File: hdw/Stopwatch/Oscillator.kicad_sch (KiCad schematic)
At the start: 12 parts, among them U401 CD4024, U402 CD4040, X401 ECS-327KE

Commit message: started sch work
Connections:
- net 16Hz_Clock: no longer names the net of U402.5 (Q3)
- net 4Hz_Clock: no longer names the net of U402.2 (Q5)
- net Count_Reset renamed Master_Reset
- no-connect marks 15 -> 17
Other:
- moved on the sheet: C401, C402, C403, C404, R401, R402, R403, R404, X401

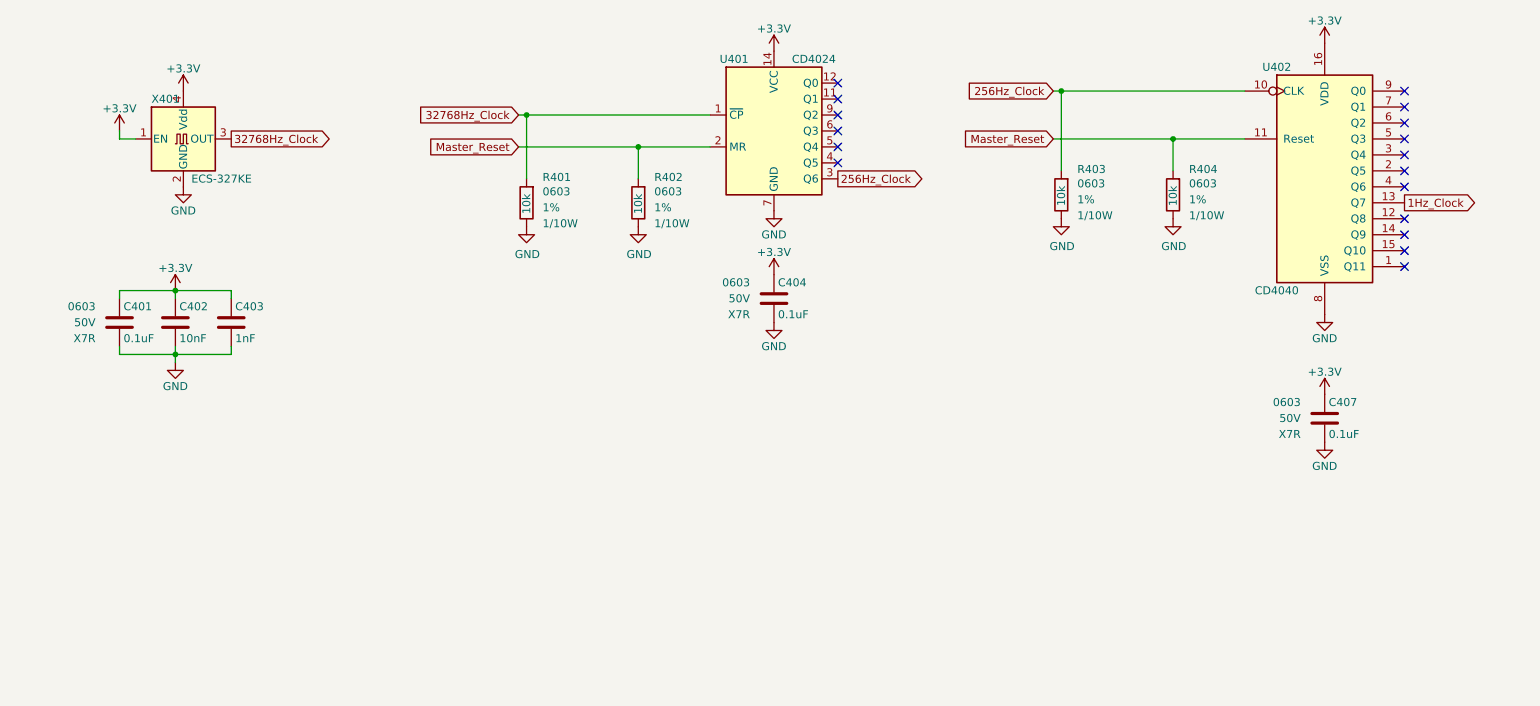
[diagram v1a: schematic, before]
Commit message: adjusted stage sheet
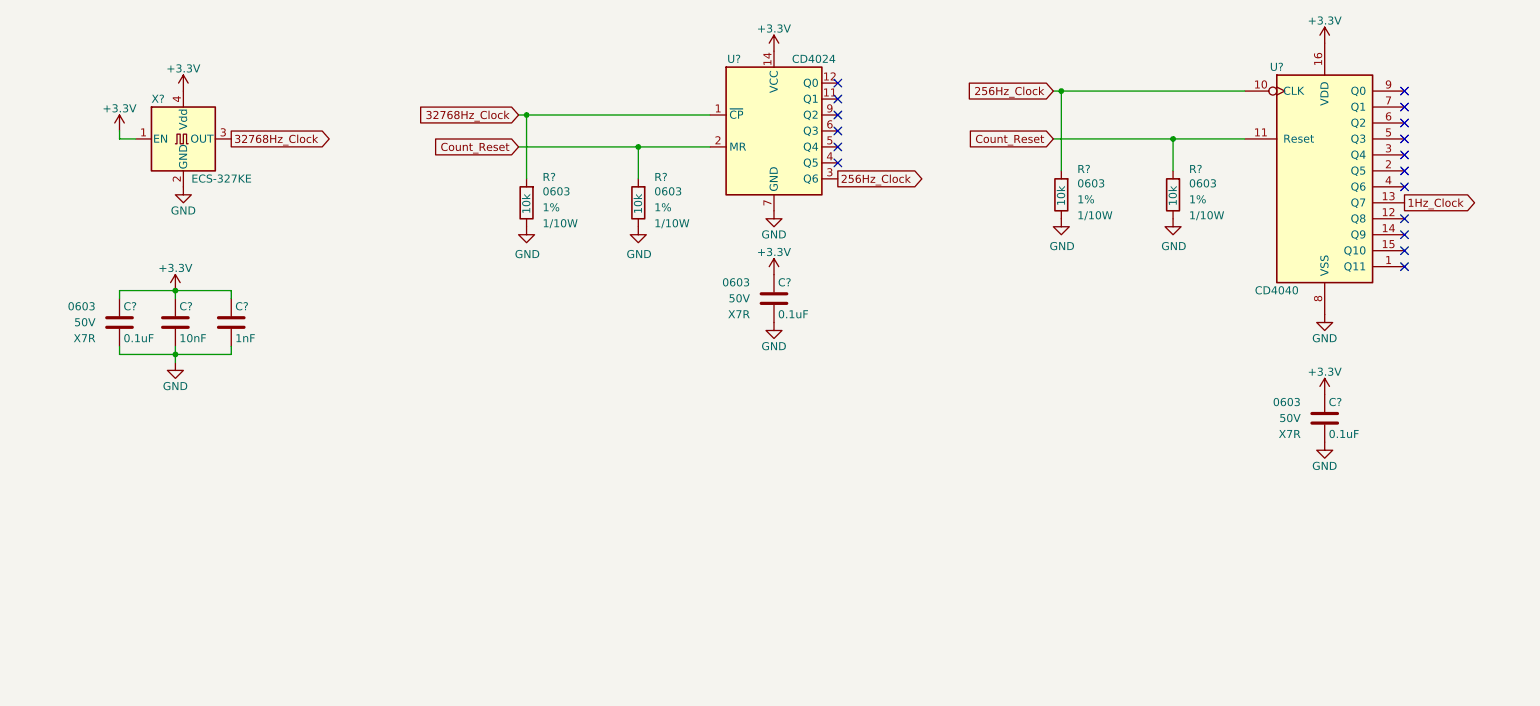
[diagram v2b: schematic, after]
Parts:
- renumbered C401 to C?, C402 to C?, C403 to C?, C404 to C?, C407 to C?, R401 to R?, R402 to R?, R404 to R?, R403 to R?, U401 to U?, U402 to U?, X401 to X?
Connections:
- net Master_Reset renamed Count_Reset

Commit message: added reset stuff
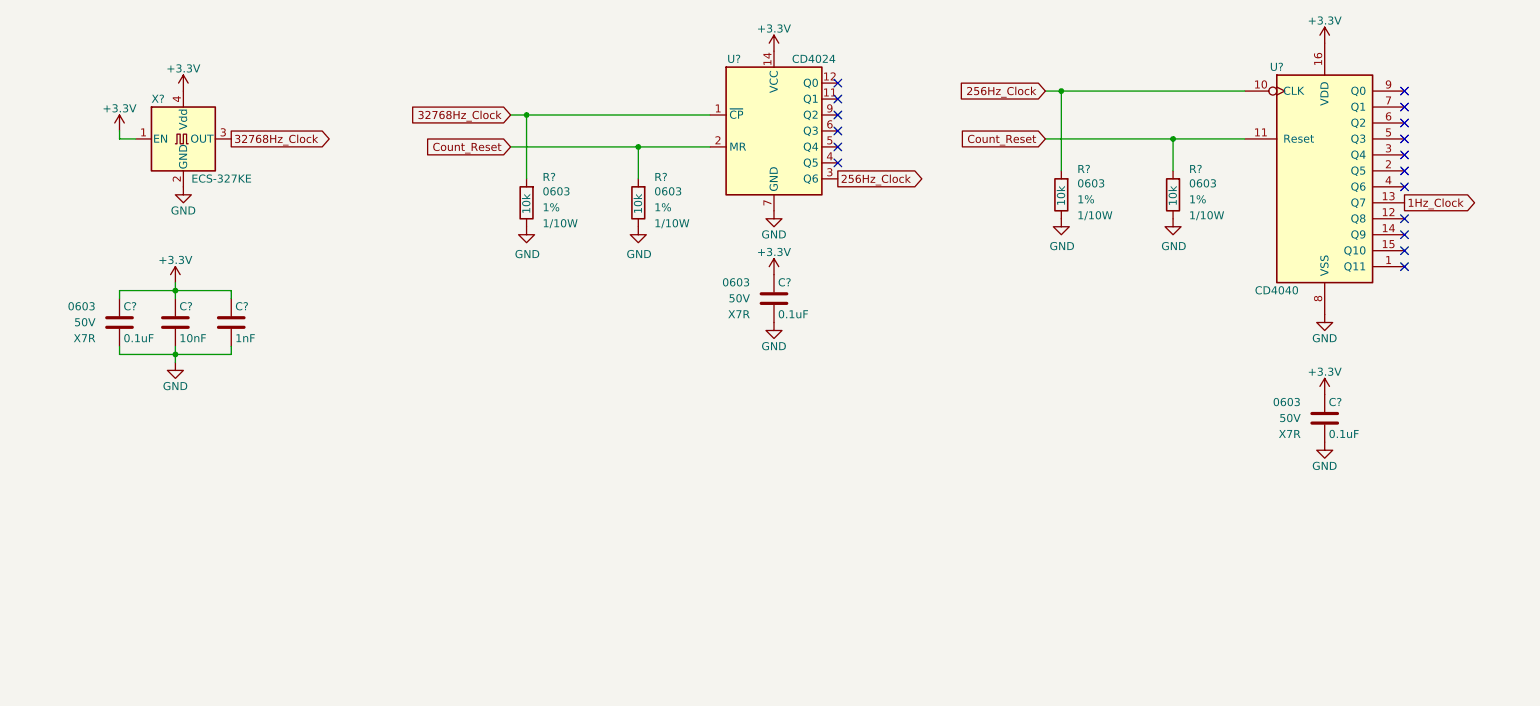
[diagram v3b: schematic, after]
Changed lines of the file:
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@@
+    (stroke (width 0) (type default))
+  )
+  (wire (pts (xy 115.57 88.9) (xy 95.25 88.9))
+    (stroke (width 0) (type default))
+  )
+  (wire (pts (xy 33.02 121.92) (xy 33.02 120.65))
+    (stroke (width 0) (type default))
+  )
+  (wire (pts (xy 41.91 121.92) (xy 41.91 120.65))
+    (stroke (width 0) (type default))
+  )
+  (wire (pts (xy 200.66 87.63) (xy 180.34 87.63))
+    (stroke (width 0) (type default))
+  )
+  (wire (pts (xy 180.34 80.01) (xy 182.88 80.01))
+    (stroke (width 0) (type default))
+  )
+  (wire (pts (xy 33.02 111.76) (xy 33.02 113.03))
+    (stroke (width 0) (type default))
+  )
+  (wire (pts (xy 41.91 111.76) (xy 50.8 111.76))
+    (stroke (width 0) (type default))
+  )
+  (wire (pts (xy 33.02 87.63) (xy 33.02 86.36))
+    (stroke (width 0) (type default))
+  )
+  (wire (pts (xy 97.79 93.98) (xy 97.79 83.82))
+    (stroke (width 0) (type default))
+  )
+  (wire (pts (xy 115.57 88.9) (xy 115.57 93.98))
     (stroke (width 0) (type default))
   )
@@
     (stroke (width 0) (type default))
   )
-  (wire (pts (xy 115.57 88.9) (xy 96.52 88.9))
-    (stroke (width 0) (type default))
-  )
-  (wire (pts (xy 33.02 121.92) (xy 33.02 120.65))
-    (stroke (width 0) (type default))
-  )
-  (wire (pts (xy 41.91 121.92) (xy 41.91 120.65))
-    (stroke (width 0) (type default))
-  )
-  (wire (pts (xy 200.66 87.63) (xy 181.61 87.63))
-    (stroke (width 0) (type default))
-  )
-  (wire (pts (xy 181.61 80.01) (xy 182.88 80.01))
-    (stroke (width 0) (type default))
-  )
-  (wire (pts (xy 33.02 111.76) (xy 33.02 113.03))
-    (stroke (width 0) (type default))
-  )
-  (wire (pts (xy 41.91 111.76) (xy 50.8 111.76))
-    (stroke (width 0) (type default))
-  )
-  (wire (pts (xy 33.02 87.63) (xy 33.02 86.36))
-    (stroke (width 0) (type default))
-  )
-  (wire (pts (xy 97.79 93.98) (xy 97.79 83.82))
-    (stroke (width 0) (type default))
-  )
-  (wire (pts (xy 115.57 88.9) (xy 115.57 93.98))
-    (stroke (width 0) (type default))
-  )
   (wire (pts (xy 127 83.82) (xy 97.79 83.82))
     (stroke (width 0) (type default))
@@
     (stroke (width 0) (type default))
   )
-  (wire (pts (xy 96.52 83.82) (xy 97.79 83.82))
+  (wire (pts (xy 95.25 83.82) (xy 97.79 83.82))
     (stroke (width 0) (type default))
   )
@@
   )
   (wire (pts (xy 212.09 87.63) (xy 200.66 87.63))
+    (stroke (width 0) (type default))
+  )
+  (wire (pts (xy 41.91 110.49) (xy 41.91 111.76))
     (stroke (width 0) (type default))
   )
@@
     )
   )
-  (global_label "Count_Reset" (shape input) (at 96.52 88.9 180)
+  (global_label "Count_Reset" (shape input) (at 95.25 88.9 180)
     (effects (font (size 1.27 1.27)) (justify right))
-    (property "Intersheetrefs" "${INTERSHEET_REFS}" (at 96.52 88.9 0)
-      (effects (font (size 1.27 1.27)) hide)
-    )
-  )
-  (global_label "32768Hz_Clock" (shape input) (at 96.52 83.82 180)
+    (property "Intersheetrefs" "${INTERSHEET_REFS}" (at 95.25 88.9 0)
+      (effects (font (size 1.27 1.27)) hide)
+    )
+  )
+  (global_label "32768Hz_Clock" (shape input) (at 95.25 83.82 180)
     (effects (font (size 1.27 1.27)) (justify right))
-    (property "Intersheetrefs" "${INTERSHEET_REFS}" (at 96.52 83.82 0)
-      (effects (font (size 1.27 1.27)) hide)
-    )
-  )
-  (global_label "256Hz_Clock" (shape input) (at 181.61 80.01 180)
+    (property "Intersheetrefs" "${INTERSHEET_REFS}" (at 95.25 83.82 0)
+      (effects (font (size 1.27 1.27)) hide)
+    )
+  )
+  (global_label "256Hz_Clock" (shape input) (at 180.34 80.01 180)
     (effects (font (size 1.27 1.27)) (justify right))
-    (property "Intersheetrefs" "${INTERSHEET_REFS}" (at 181.61 80.01 0)
-      (effects (font (size 1.27 1.27)) hide)
-    )
-  )
-  (global_label "Count_Reset" (shape input) (at 181.61 87.63 180)
+    (property "Intersheetrefs" "${INTERSHEET_REFS}" (at 180.34 80.01 0)
+      (effects (font (size 1.27 1.27)) hide)
+    )
+  )
+  (global_label "Count_Reset" (shape input) (at 180.34 87.63 180)
     (effects (font (size 1.27 1.27)) (justify right))
-    (property "Intersheetrefs" "${INTERSHEET_REFS}" (at 181.61 87.63 0)
+    (property "Intersheetrefs" "${INTERSHEET_REFS}" (at 180.34 87.63 0)
       (effects (font (size 1.27 1.27)) hide)
     )
@@
     )
   )
-  (symbol (lib_id "Incrementor-rescue:+3.3V-power") (at 41.91 111.76 0) (unit 1)
-    (in_bom yes) (on_board yes) (dnp no)
-    (property "Reference" "#PWR?" (at 41.91 115.57 0)
-      (effects (font (size 1.27 1.27)) hide)
-    )
-    (property "Value" "+3.3V" (at 41.91 108.204 0)
+  (symbol (lib_id "Incrementor-rescue:+3.3V-power") (at 41.91 110.49 0) (unit 1)
+    (in_bom yes) (on_board yes) (dnp no)
+    (property "Reference" "#PWR?" (at 41.91 114.3 0)
+      (effects (font (size 1.27 1.27)) hide)
+    )
+    (property "Value" "+3.3V" (at 41.91 106.934 0)
       (effects (font (size 1.27 1.27)))
     )
-    (property "Footprint" "" (at 41.91 111.76 0)
-      (effects (font (size 1.27 1.27)) hide)
-    )
-    (property "Datasheet" "" (at 41.91 111.76 0)
-      (effects (font (size 1.27 1.27)) hide)
-    )
+    (property "Footprint" "" (at 41.91 110.49 0)
+      (effects (font (size 1.27 1.27)) hide)
+    )
+    (property "Datasheet" "" (at 41.91 110.49 0)
+      (effects (font (size 1.27 1.27)) hide)
+    )

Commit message: added some more junk
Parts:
- added C?: 0.1uF, Capacitors_SMD:C_0603, symbol Custom_Library:C_Custom
- added R? (x2): 10k, Resistors_SMD:R_0603, symbol Custom_Library:R_Custom
- added U?: 74LVC1G97, Package_TO_SOT_SMD:SOT-363_SC-70-6, symbol Custom Library:74LVC1G97_Power_AND
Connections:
- net +3V3: now also C?.1
- net 1Hz_Clock: now also R?.1, U?.4; no longer U?.13 (Q7)
- net GND: now also C?.2, R?.2, R?.2, U?.1 (GND), U?.2 (GND)
- new net +3.3V: U?.5 (VCC)
- new net 1Hz_Clock_SRC: R?.1, U?.13 (Q7), U?.3
- new net Count_Enable: U?.6

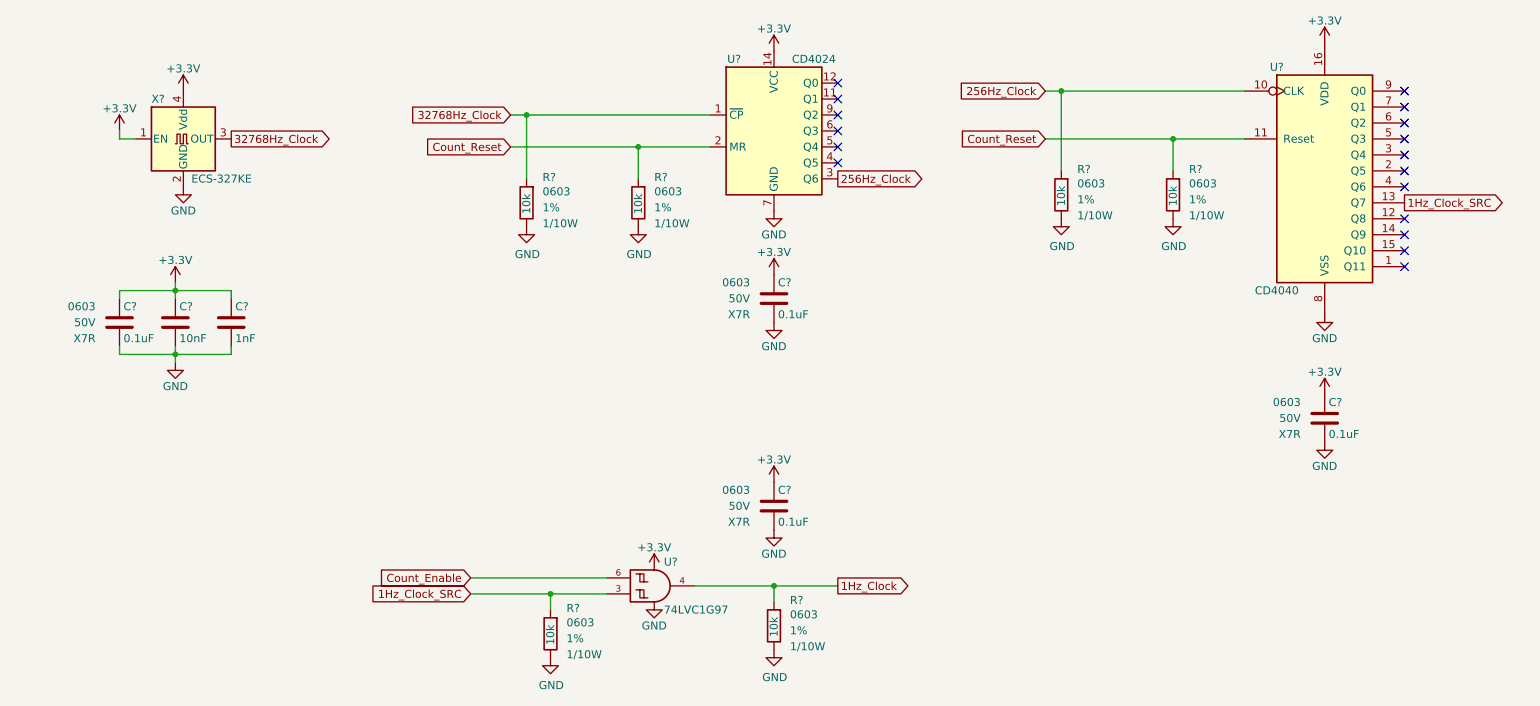
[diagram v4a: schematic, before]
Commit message: Assigned some digikey pns
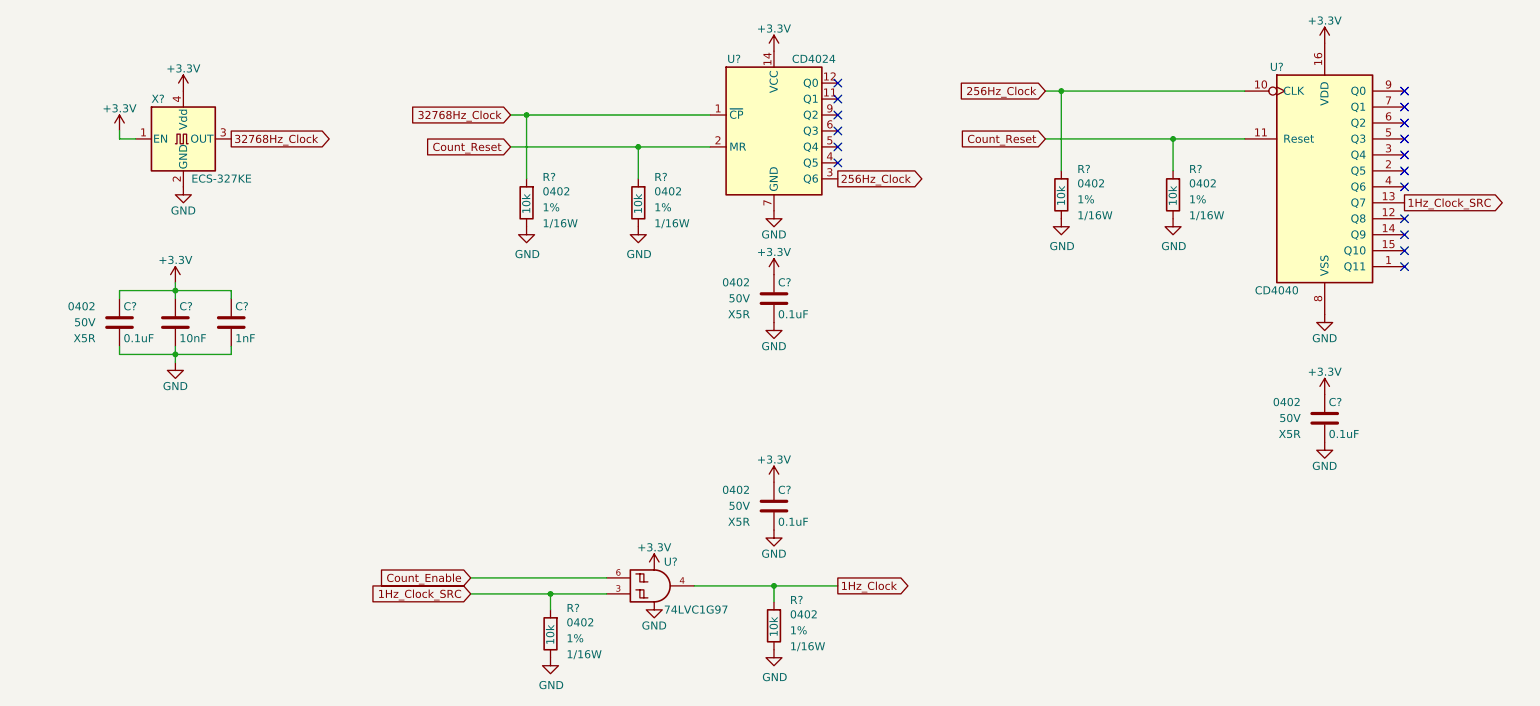
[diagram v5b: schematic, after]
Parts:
- C? (x4): footprint Capacitors_SMD:C_0603 -> Capacitors_SMD:C_0402; Dielectric X7R -> X5R; Digi-Key PN 311-1344-1-ND -> 490-10697-1-ND; display_footprint 0603 -> 0402
- C?: footprint Capacitors_SMD:C_0603 -> Capacitors_SMD:C_0402; Dielectric X7R -> X5R; Digi-Key PN 1276-1921-1-ND -> 445-12201-1-ND; display_footprint 0603 -> (none)
- C?: footprint Capacitors_SMD:C_0603 -> Capacitors_SMD:C_0402; Dielectric X7R -> X5R; Digi-Key PN 1276-1018-1-ND -> 445-7376-1-ND; display_footprint 0603 -> 0402
- R? (x6): footprint Resistors_SMD:R_0603 -> Resistors_SMD:R_0402; Digi-Key PN RMCF0603FT10K0CT-ND -> RMCF0402FT10K0CT-ND; Wattage 1/10W -> 1/16W; display_footprint 0603 -> 0402
- U?: footprint Package_TO_SOT_SMD:SOT-363_SC-70-6 -> (none); Digi-Key PN (none) -> 296-29875-1-ND
- X?: footprint Custom Footprints Library:ECS-327KE -> (none)

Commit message: added proper power sequencing, discharge
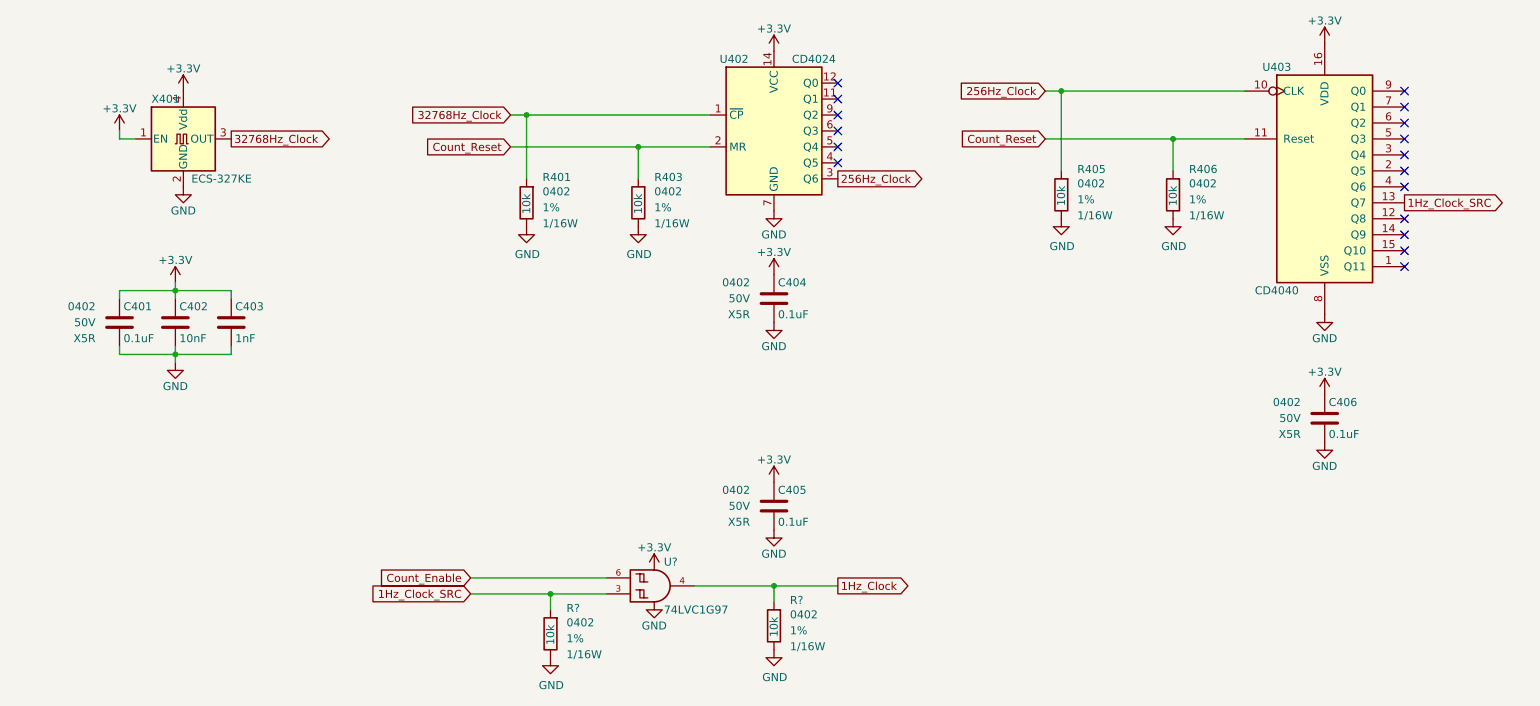
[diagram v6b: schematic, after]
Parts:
- C402: renamed from C?; display_footprint (none) -> 0402
- U?: footprint (none) -> Package_SON:Fairchild_MicroPak2-6_1.0x1.0mm_P0.35mm
- X401: renamed from X?; footprint (none) -> Oscillator:Oscillator_SMD_Abracon_ASE-4Pin_3.2x2.5mm
- gave numbers to parts that had none: 11

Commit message: lots and lots of routing
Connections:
- net +3.3V: now also C401.1, C402.1, C403.1, C404.1, C405.1, C406.1, U402.14 (VCC), U403.16 (VDD), X401.4 (Vdd)
- removed net +3V3: C401.1, C402.1, C403.1, C404.1, C405.1, C406.1, U402.14 (VCC), U403.16 (VDD), X401.1 (EN), X401.4 (Vdd)
- new net POS3P3_PGOOD: X401.1 (EN)
